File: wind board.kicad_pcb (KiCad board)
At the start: 2 copper layers, 70.1 x 65.1 mm, 111 parts, among them J1 USB_C_Receptacle_USB2.0_14P, J2 Conn_01x06_MountingPin, J3 Conn_01x06_MountingPin, J4 12V -, J5 12V +, J6 Conn_01x06_MountingPin, Q1 AONR21321, U1 CH334R, U2 FT232RNL, U3 FT232RNL, U4 ZT3222F, U5 ZT3222F, U6 TPS565242, U7 FT232RNL, U8 ZT3222F, Y1 12MHz

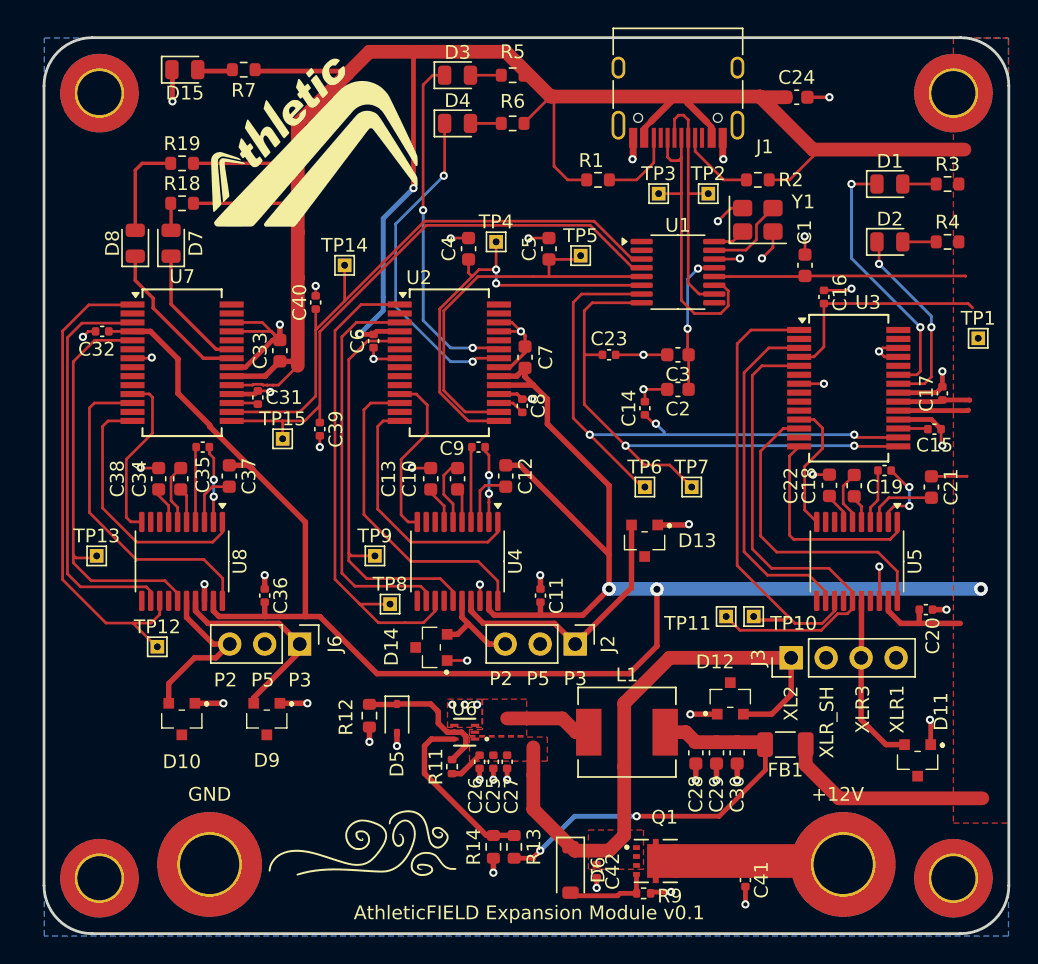
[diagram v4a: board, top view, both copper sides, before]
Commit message: add usb-c-pd routing
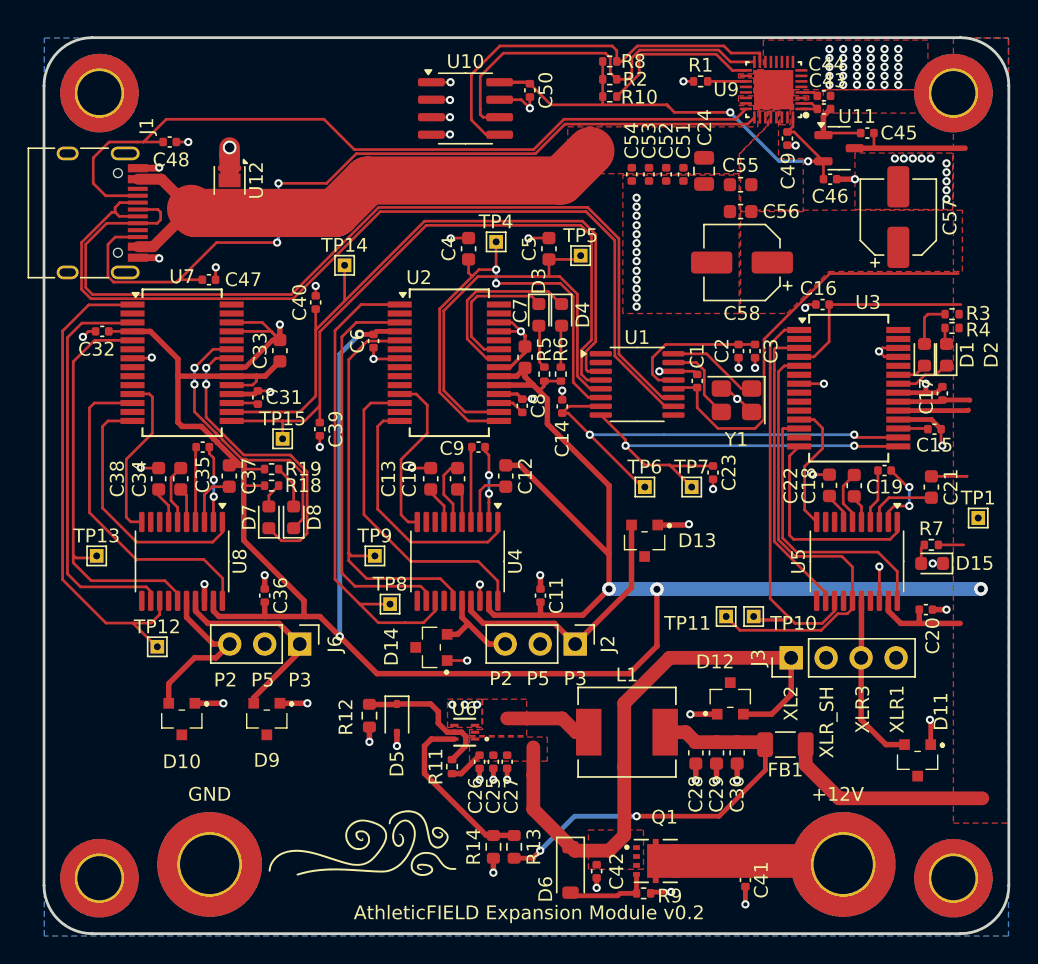
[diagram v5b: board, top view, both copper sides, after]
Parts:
- removed the G*** at (118.6, 57.6)
- removed TP2, TP3: TestPoint, TestPoint:TestPoint_THTPad_1.0x1.0mm_Drill0.5mm
- added C43: 10uF, Capacitor_SMD:C_0402_1005Metric, F.Cu at (155.6, 55.1)
- added C44: 10uF, Capacitor_SMD:C_0402_1005Metric, F.Cu at (155.6, 54.2)
- added C45: 1uF, Capacitor_SMD:C_0402_1005Metric, F.Cu at (158.8, 56.9)
- added C46: 1uF, Capacitor_SMD:C_0402_1005Metric, F.Cu at (156.1, 60.2)
- added C47: 330pF, Capacitor_SMD:C_0402_1005Metric, F.Cu at (111.0, 67.5)
- added C48: 330pF, Capacitor_SMD:C_0402_1005Metric, F.Cu at (108.1, 57.5)
- added C49: 10uF, Capacitor_SMD:C_0402_1005Metric, F.Cu at (152.9, 57.3)
- added C50: 0.1uF, Capacitor_SMD:C_0402_1005Metric, F.Cu at (134.2, 53.8)
- added C51: 0.01uF, Capacitor_SMD:C_0402_1005Metric, F.Cu at (145.4, 59.9)
- added C52: 0.01uF, Capacitor_SMD:C_0402_1005Metric, F.Cu at (144.2, 59.9)
- added C53: 0.01uF, Capacitor_SMD:C_0402_1005Metric, F.Cu at (142.9, 59.9)
- added C54: 0.01uF, Capacitor_SMD:C_0402_1005Metric, F.Cu at (141.7, 59.9)
- added C55: 10uF / 10V, Capacitor_SMD:C_0603_1608Metric, F.Cu at (149.6, 60.6)
- added C56: 10uF / 10V, Capacitor_SMD:C_0603_1608Metric, F.Cu at (149.6, 62.6)
- added C57: 100uF / 10V, Capacitor_SMD:CP_Elec_5x5.4, F.Cu at (161.0, 63.0)
- added C58: 100uF / 10V, Capacitor_SMD:CP_Elec_5x5.4, F.Cu at (149.7, 66.3)
- added R10: 10K, Resistor_SMD:R_0402_1005Metric, F.Cu at (140.1, 54.2)
- added R8: 10K, Resistor_SMD:R_0402_1005Metric, F.Cu at (140.1, 51.7)
- added U10: AT24C512C-SSHM, Package_SO:SOIC-8_3.9x4.9mm_P1.27mm, F.Cu at (129.6, 55.1)
- added U11: XC6206PxxxMR, Package_TO_SOT_SMD:SOT-23-3, F.Cu at (156.7, 58.0)
- added U12: TVS2200DRV, Package_SON:WSON-6-1EP_2x2mm_P0.65mm_EP1x1.6mm, F.Cu at (112.5, 60.3)
- added U9: PTPS25751SRSMR, TPS25751S:RSM0032B-IPC_A, F.Cu at (151.9, 53.8)
- C1, C2, C3: footprint Capacitor_SMD:C_0603_1608Metric -> Capacitor_SMD:C_0402_1005Metric
- C24: value 10uF -> 4.7uF 25V; footprint Capacitor_SMD:C_0603_1608Metric -> Capacitor_SMD:C_0805_2012Metric
- D1, D15, D2, D3, D4, D7, D8: footprint LED_SMD:LED_0805_2012Metric -> LED_SMD:LED_0603_1608Metric
- R1: value 22K -> 0; footprint Resistor_SMD:R_0603_1608Metric -> Resistor_SMD:R_0402_1005Metric
- R18, R19, R3, R4, R5, R6, R7: footprint Resistor_SMD:R_0603_1608Metric -> Resistor_SMD:R_0402_1005Metric
- R2: value 22K -> 10K; footprint Resistor_SMD:R_0603_1608Metric -> Resistor_SMD:R_0402_1005Metric
- moved D15 65.0 mm to (163.4, 88.2), turned to 180 degrees
- moved R7 60.7 mm to (163.4, 86.8)
- moved J1 44.3 mm to (101.7, 62.7), turned to -90 degrees
- moved R19 23.1 mm to (115.5, 81.3), turned to 180 degrees
- moved D8 23.0 mm to (117.1, 84.8)
- moved R5 21.8 mm to (135.3, 74.4), turned to -90 degrees
- moved R18 21.5 mm to (115.5, 82.5), turned to 180 degrees
- moved D7 21.1 mm to (115.3, 84.8)
- moved R6 18.5 mm to (136.5, 74.4), turned to -90 degrees
- moved D3 18.4 mm to (134.9, 70.1), turned to -90 degrees
- moved D4 15.8 mm to (136.6, 70.1), turned to -90 degrees
- moved Y1 13.2 mm to (149.2, 76.3), turned to 180 degrees
- moved TP1 13.0 mm to (166.8, 84.8)
- moved R2 13.0 mm to (140.1, 53.0), turned to 0 degrees
- moved D1 12.7 mm to (162.9, 73.0), turned to 90 degrees
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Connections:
- net Net-(U1-DMU-) renamed /USB_C_PD/DM-
- net Net-(U1-DPU+) renamed /USB_C_PD/DP+
- C2 pad 1: Net-(U1-VDD33) -> unconnected-(U1-VDD33-Pad13)
- C24 pad 1: +5V -> Net-(C24-Pad1)
- C3 pad 1: Net-(U1-VDD33) -> unconnected-(U1-VDD33-Pad13)
- J1 pad A4: +5V -> Net-(C24-Pad1)
- J1 pad A5: Net-(J1-CC1) -> /USB_C_PD/CC1
- J1 pad A9: +5V -> Net-(C24-Pad1)
- J1 pad B4: +5V -> Net-(C24-Pad1)
- J1 pad B5: Net-(J1-CC2) -> /USB_C_PD/CC2
- J1 pad B9: +5V -> Net-(C24-Pad1)
- R1 pad 1: +5V -> ~
- R1 pad 2: Net-(J1-CC2) -> Net-(U9-VSYS)
- R2 pad 1: +5V -> +3V3
- R2 pad 2: Net-(J1-CC1) -> Net-(U10-SCL)
- U1 pad 13: Net-(U1-VDD33) -> unconnected-(U1-VDD33-Pad13)
- U7 pad 22: Net-(D8-K) -> Net-(D7-K)
- U7 pad 23: Net-(D7-K) -> Net-(D8-K)
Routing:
- net +5V: track 368.8 -> 276.2 mm
- net /USB_C_PD/CC2: track 0.00 -> 61.1 mm, vias 0 -> 2
- net /USB_C_PD/CC1: track 0.00 -> 57.6 mm
- net /USB_C_PD/DM-: track 18.1 -> 67.3 mm
- net /USB_C_PD/DP+: track 23.0 -> 67.7 mm
- net Net-(C24-Pad1): track 0.00 -> 40.7 mm
- net +3V3: track 0.00 -> 35.7 mm, vias 0 -> 2
- net Net-(U10-SDA): track 0.00 -> 29.8 mm
- net Net-(U10-SCL): track 0.00 -> 28.2 mm
- net Net-(D1-K): track 19.4 -> 2.17 mm, vias 2 -> 0
- net Net-(D3-K): track 25.3 -> 10.3 mm, vias 2 -> 0
- net Net-(D7-K): track 9.24 -> 22.6 mm, vias 0 -> 2
- net Net-(U9-I2Cc_IRQ_N): track 0.00 -> 11.9 mm
- net Net-(U1-DM1-): track 45.5 -> 33.7 mm, vias 3 -> 2
- net Net-(D4-K): track 24.0 -> 13.1 mm, vias 2 -> 0
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- added copper zone on F.Cu, net Net-(C24-Pad1)
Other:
- board text added: "AthleticFIELD Expansion Module v0.2"
- board text removed: "AthleticFIELD Expansion Module v0.1"

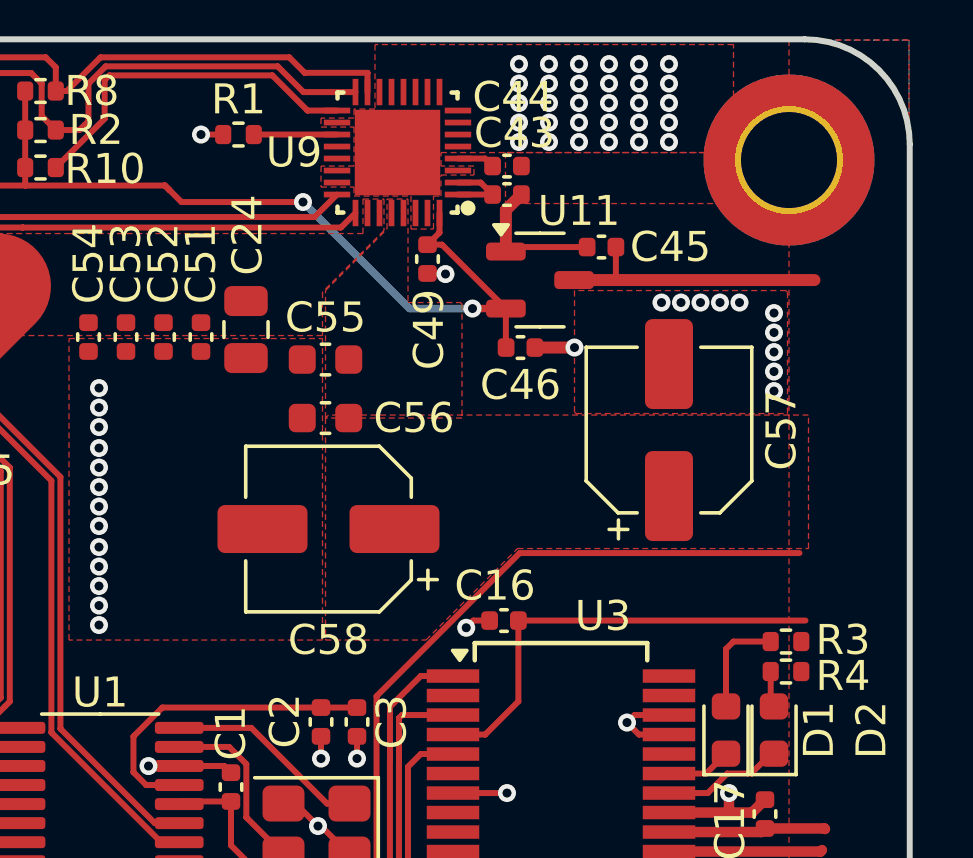
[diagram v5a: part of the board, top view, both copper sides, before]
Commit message: update capacitors
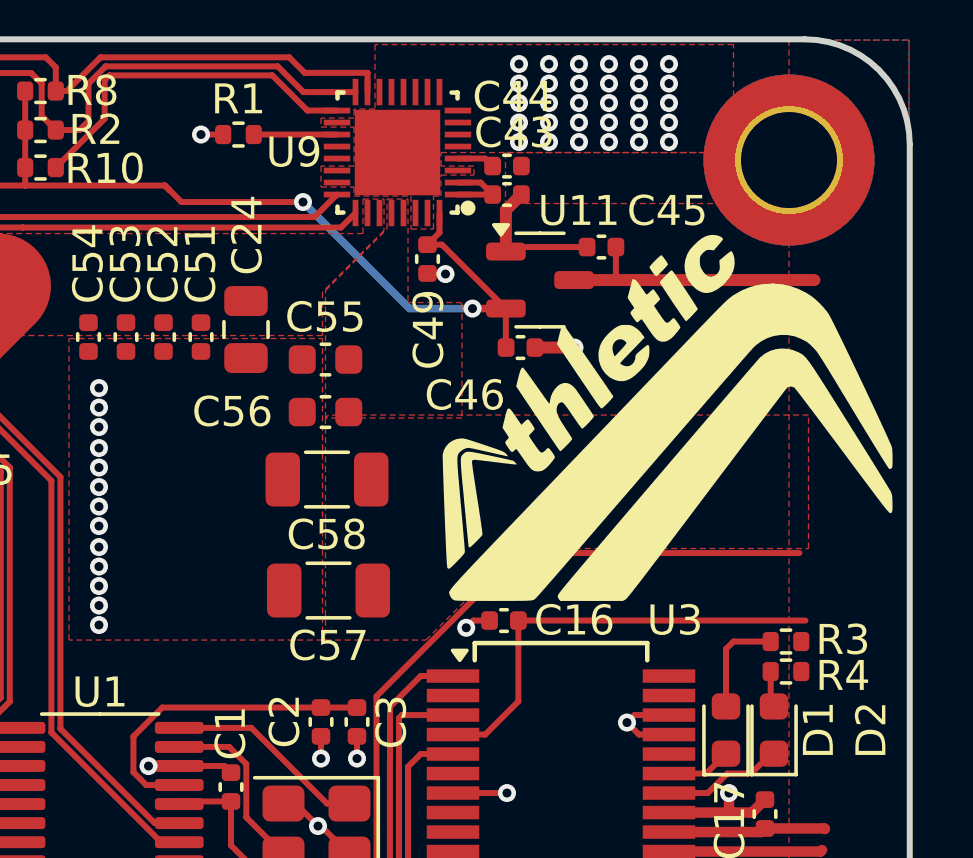
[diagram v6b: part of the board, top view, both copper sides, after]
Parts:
- added G***: LOGO, logos:athletic Square, F.Cu at (160.9, 62.6)
- C57, C58: footprint Capacitor_SMD:CP_Elec_5x5.4 -> Capacitor_SMD:C_1206_3216Metric
- moved C57 12.5 mm to (149.7, 68.3), turned to 180 degrees
- moved C58 1.65 mm to (149.6, 64.7)
- moved C56 0.20 mm to (149.6, 62.4)
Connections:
- C2 pad 1: unconnected-(U1-VDD33-Pad13) -> Net-(U1-VDD33)
- C3 pad 1: unconnected-(U1-VDD33-Pad13) -> Net-(U1-VDD33)
- U1 pad 13: unconnected-(U1-VDD33-Pad13) -> Net-(U1-VDD33)
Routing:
- net unconnected-(U1-VDD33-Pad13): track 10.7 -> 0.00 mm
- net Net-(U1-VDD33): track 0.00 -> 10.7 mm
- net ~: vias 119 -> 109

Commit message: aaahhhhhh
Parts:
- C47, C48: footprint Capacitor_SMD:C_0402_1005Metric -> Capacitor_SMD:C_0603_1608Metric
- C50: value 0.1uF -> 100nF
- moved C23 7.89 mm to (139.9, 79.6)
- moved TP13 7.82 mm to (107.3, 94.0)
- moved C40 7.77 mm to (116.4, 76.6)
- moved C3 6.44 mm to (144.3, 71.4), turned to 90 degrees
- moved C2 6.35 mm to (143.2, 71.4), turned to 90 degrees
- moved D13 4.72 mm to (139.3, 89.9)
- moved Y1 3.87 mm to (148.9, 72.5)
- moved C39 3.80 mm to (115.2, 78.4)
- moved C14 2.94 mm to (137.4, 79.6), turned to -90 degrees
- moved D11 2.53 mm to (160.8, 100.4)
- moved TP12 2.31 mm to (104.9, 94.0)
- moved C35 2.18 mm to (110.0, 81.8), turned to 90 degrees
- moved C36 1.73 mm to (113.6, 91.5)
- moved C11 1.37 mm to (133.8, 91.1)
- moved TP15 1.20 mm to (117.5, 79.1)
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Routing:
- net +5V: track 276.2 -> 262.2 mm
- net Net-(U1-VDD33): track 10.7 -> 5.24 mm
- net Net-(J2-Pin_1): track 19.6 -> 14.9 mm
- net Net-(U7-RTS): track 28.5 -> 24.7 mm
- net Net-(J3-Pin_3): track 12.5 -> 9.11 mm
- net Net-(U7-RXD): track 29.3 -> 25.9 mm
- net Net-(U1-XO): track 6.00 -> 3.05 mm
- net Net-(U1-DP1+): track 32.0 -> 29.3 mm
- net Net-(U8-C1-): track 5.46 -> 2.85 mm
- net Net-(U7-CBUS4): track 24.0 -> 21.8 mm
- net Net-(U7-TXD): track 35.6 -> 33.5 mm
- net /USB_C_PD/DP+: track 67.7 -> 65.9 mm
- net Net-(U3-CBUS4): track 20.6 -> 18.8 mm
- net /USB_C_PD/DM-: track 67.3 -> 65.7 mm
- net /DM3-: track 50.7 -> 49.2 mm
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
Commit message: update bom
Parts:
- J2, J6: footprint Connector_PinHeader_2.54mm:PinHeader_1x03_P2.54mm_Vertical -> Connector_PinHeader_2.54mm:PinHeader_1x03_P2.54mm_Horizontal
- J3: footprint Connector_PinHeader_2.54mm:PinHeader_1x04_P2.54mm_Vertical -> Connector_PinHeader_2.54mm:PinHeader_1x04_P2.54mm_Horizontal
- moved C20 13.0 mm to (150.4, 88.0), turned to 0 degrees
- moved U5 9.86 mm to (149.2, 83.6)
- moved C21 9.79 mm to (153.7, 83.5), turned to 90 degrees
- moved C18 9.74 mm to (149.1, 78.2)
- moved C22 9.49 mm to (147.5, 78.2)
- moved C19 9.30 mm to (150.8, 79.0), turned to 0 degrees
- moved D13 8.43 mm to (142.4, 82.0)
- moved TP7 6.62 mm to (139.4, 83.1)
- moved J6 5.45 mm to (111.9, 96.6), turned to 90 degrees
- moved TP10 5.28 mm to (145.3, 93.2)
- moved TP6 5.27 mm to (137.3, 83.1)
- moved R7 5.08 mm to (164.9, 82.0)
- moved C36 4.96 mm to (108.8, 92.5), turned to 0 degrees
- moved D15 4.70 mm to (163.4, 83.4)
- moved J3 3.10 mm to (153.2, 98.1)
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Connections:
- D10 pad 2: Net-(J6-Pin_3) -> Net-(J6-Pin_1)
- D13 pad 2: Net-(J2-Pin_1) -> Net-(J2-Pin_3)
- D14 pad 2: Net-(J2-Pin_3) -> Net-(J2-Pin_1)
- D9 pad 2: Net-(J6-Pin_1) -> Net-(J6-Pin_3)
- U4 pad 16: Net-(J2-Pin_3) -> Net-(J2-Pin_1)
- U4 pad 17: Net-(J2-Pin_1) -> Net-(J2-Pin_3)
- U8 pad 16: Net-(J6-Pin_3) -> Net-(J6-Pin_1)
- U8 pad 17: Net-(J6-Pin_1) -> Net-(J6-Pin_3)
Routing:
- net +5V: track 262.2 -> 239.7 mm, vias 5 -> 7
- net Net-(J2-Pin_3): track 7.39 -> 27.5 mm
- net Net-(U3-CBUS3): track 15.3 -> 3.24 mm
- net Net-(J3-Pin_3): track 9.11 -> 18.8 mm
- net Net-(U3-RTS): track 22.0 -> 30.2 mm
- net Net-(J6-Pin_3): track 11.2 -> 18.5 mm
- net Net-(U3-TXD): track 30.1 -> 37.5 mm
- net Net-(U3-CBUS4): track 18.8 -> 12.2 mm
- net Net-(J2-Pin_1): track 14.9 -> 9.94 mm
- net Net-(U7-RTS): track 24.7 -> 29.5 mm
- net Net-(U5-C1+): track 6.44 -> 1.81 mm, vias 2 -> 0
- net Net-(U7-CBUS3): track 16.5 -> 21.0 mm
- net Net-(U8-C1+): track 4.68 -> 7.12 mm
- net Net-(U7-RXD): track 25.9 -> 28.2 mm
- net Net-(U1-DM1-): track 34.7 -> 32.8 mm
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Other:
- board text added: "1"
- board text added: "2"
- board text added: "3"
- board text added: "SH"
- board text removed: "P2"
- board text removed: "P3"
- board text removed: "P5"
- board text removed: "XL2"
- board text removed: "XLR1"
- board text removed: "XLR3"
- board text removed: "XLR_SH"
